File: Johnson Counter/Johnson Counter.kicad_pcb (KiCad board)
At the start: 2 copper layers, 149.9 x 114.3 mm, 52 parts, among them J101 USB_A, SW601 SW_Push, U201 74HC74, U301 74HC74, U401 74HC74, U501 74HC74, U601 LM555xM, U701 4081, U702 4081

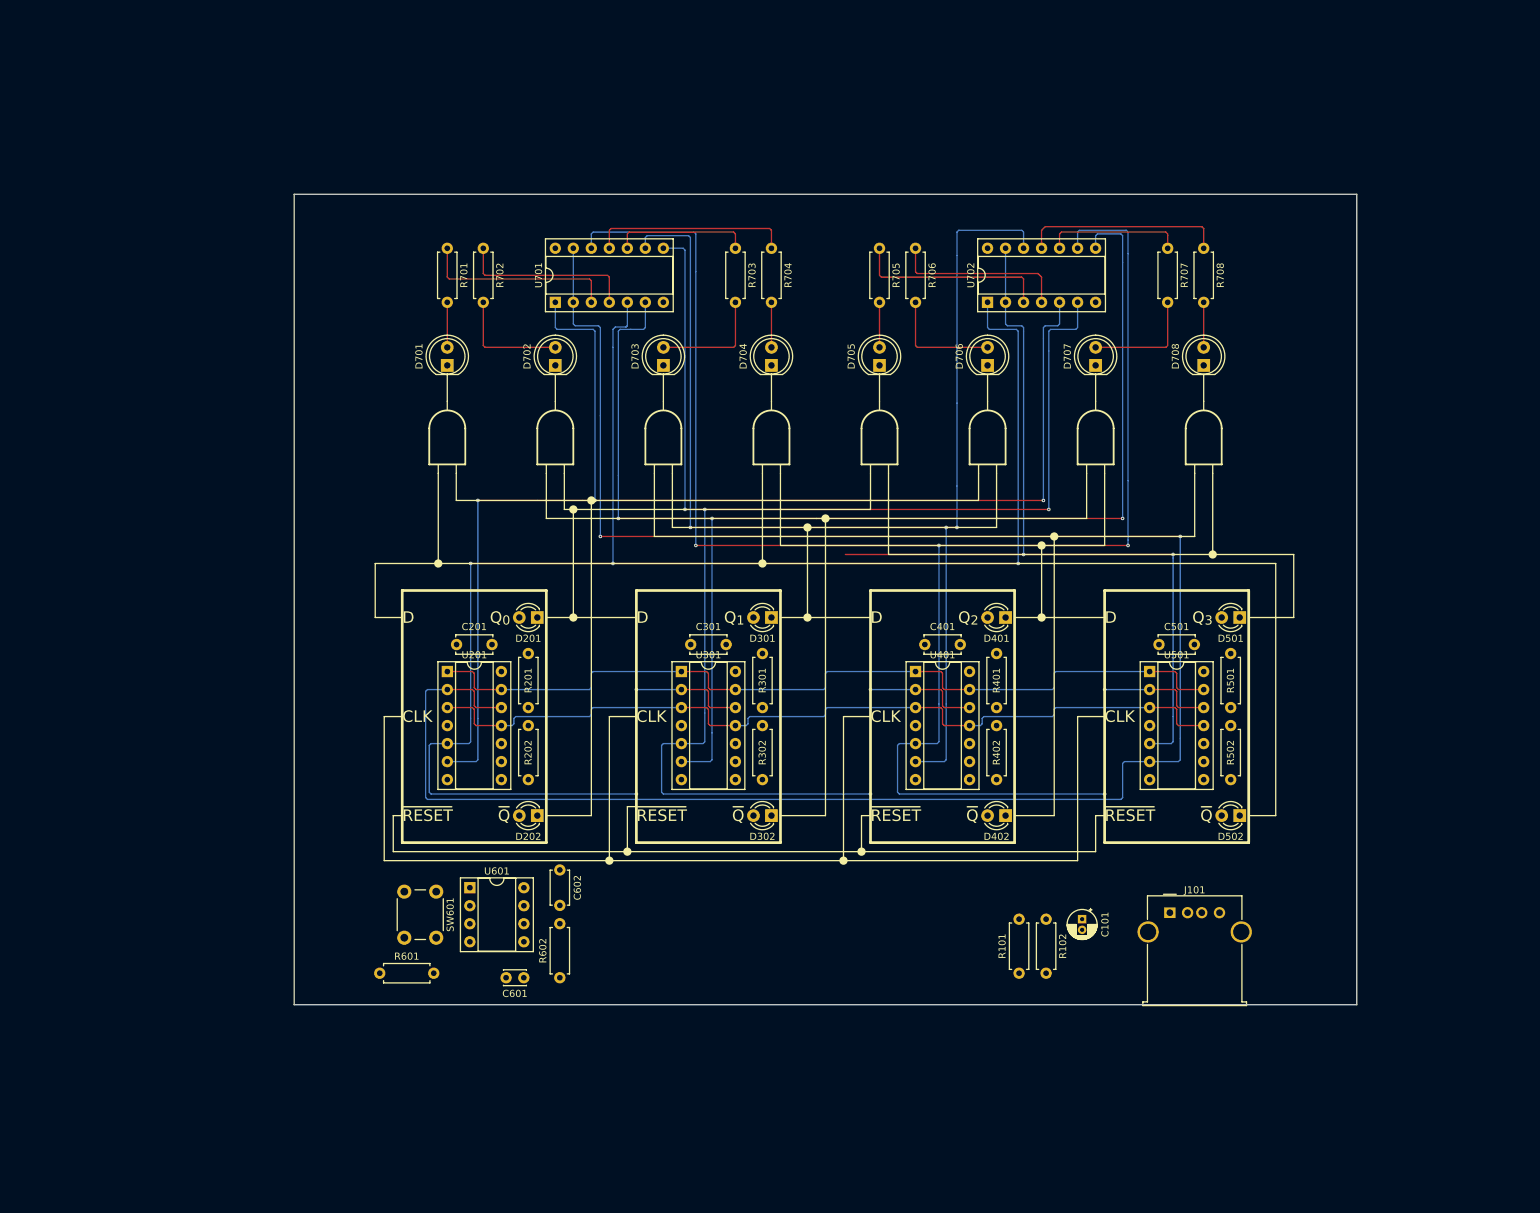
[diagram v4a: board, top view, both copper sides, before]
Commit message: Finishing routing, silkscreen and mounting
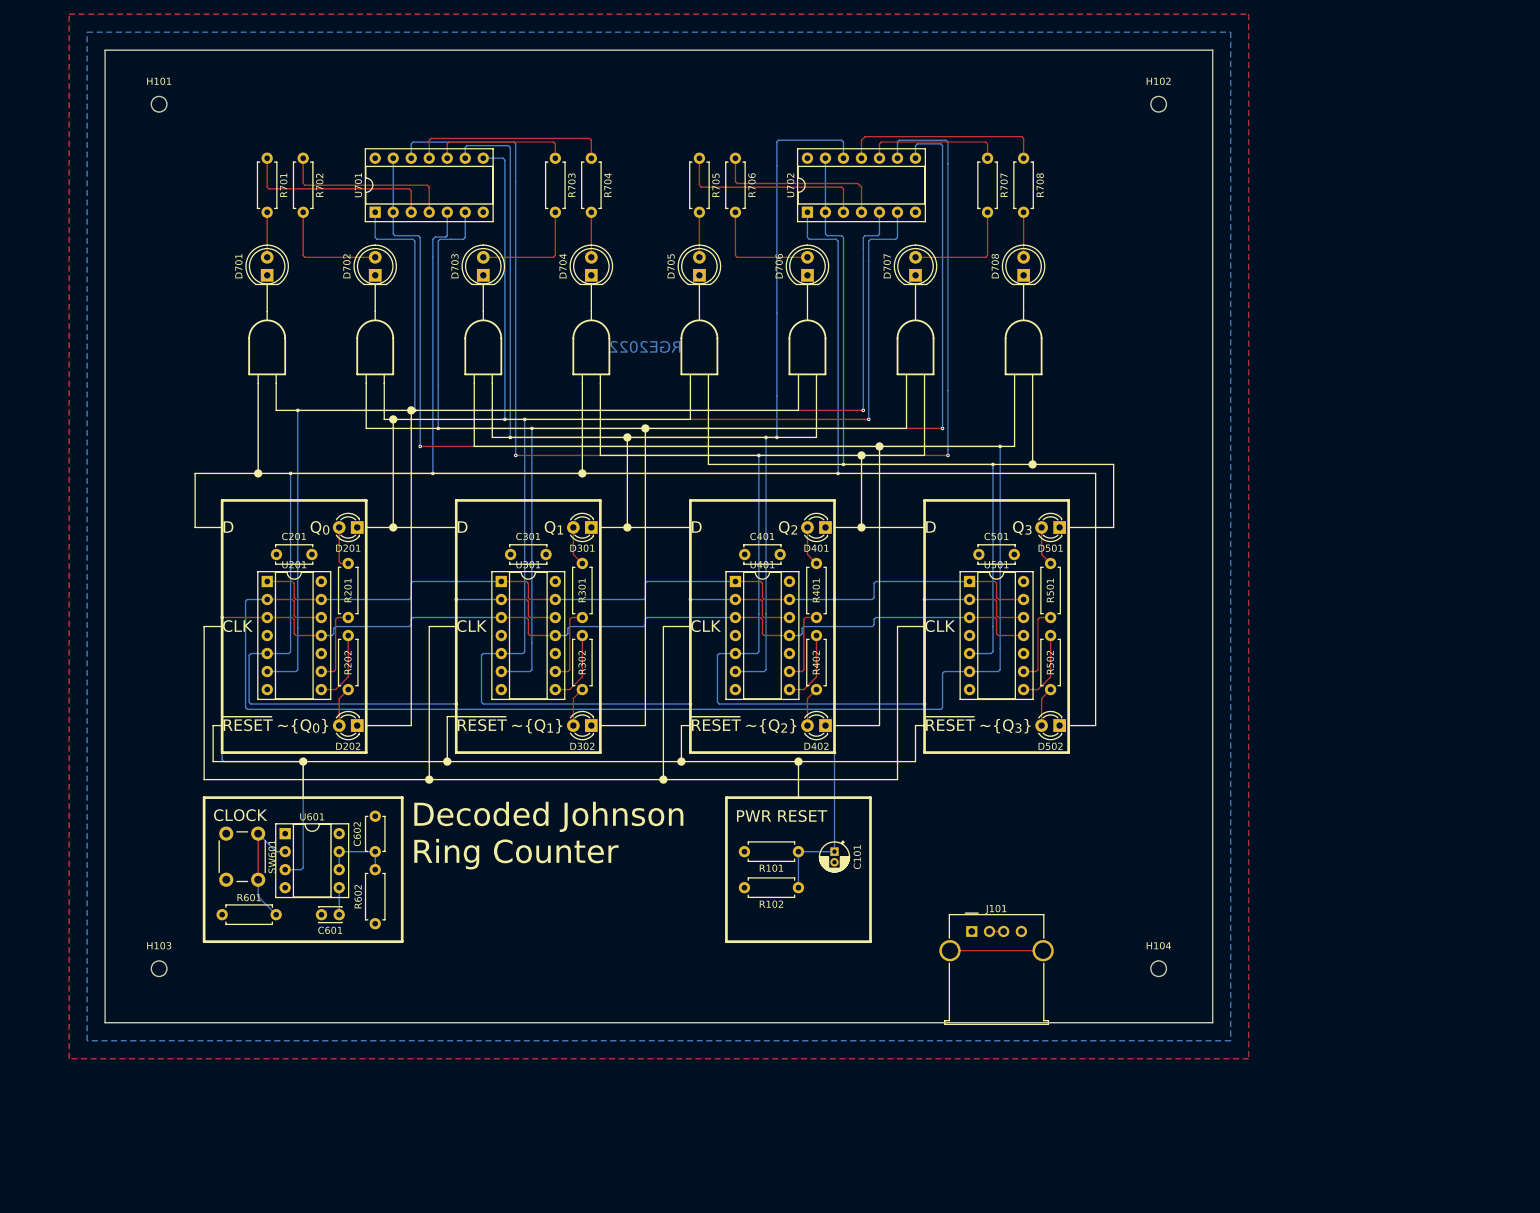
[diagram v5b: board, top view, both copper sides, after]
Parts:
- added H101: MountingHole, MountingHole:MountingHole_2.2mm_M2, F.Cu at (85.1, 31.8)
- added H102: MountingHole, MountingHole:MountingHole_2.2mm_M2, F.Cu at (226.1, 31.8)
- added H103: MountingHole, MountingHole:MountingHole_2.2mm_M2, F.Cu at (85.1, 153.7)
- added H104: MountingHole, MountingHole:MountingHole_2.2mm_M2, F.Cu at (226.1, 153.7)
- moved C101 36.2 mm to (180.3, 137.2)
- moved R101 35.5 mm to (175.3, 137.2), turned to 180 degrees
- moved R102 35.2 mm to (175.3, 142.2), turned to 180 degrees
- moved D202 28.4 mm to (113.0, 119.4)
- moved D402 28.4 mm to (179.1, 119.4)
- moved D502 28.4 mm to (212.1, 119.4)
- moved C201 28.4 mm to (101.6, 95.2)
- moved C301 28.4 mm to (134.7, 95.2)
- moved C401 28.4 mm to (167.7, 95.2)
- moved C501 28.4 mm to (200.7, 95.2)
- moved D201 28.4 mm to (113.0, 91.4)
- moved D401 28.4 mm to (179.1, 91.4)
- moved D501 28.4 mm to (212.1, 91.4)
- moved R301 28.4 mm to (144.8, 104.1)
- moved R501 28.4 mm to (210.8, 104.1)
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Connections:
- C602 pad 1: GND -> Net-(R602-Pad2)
- C602 pad 2: Net-(C602-Pad2) -> GND
- R101 pad 1: +5V -> /~{RESET}
- R101 pad 2: /~{RESET} -> +5V
- R602 pad 2: Net-(C602-Pad2) -> Net-(R602-Pad2)
- U601 pad 6: Net-(C602-Pad2) -> Net-(R602-Pad2)
- U601 pad 7: Net-(C602-Pad2) -> Net-(R602-Pad2)
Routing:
- net /CLOCK: track 121.5 -> 176.9 mm, vias 0 -> 1
- net /~{RESET}: track 122.4 -> 168.1 mm, vias 0 -> 2
- net /Q_{3}: track 121.5 -> 96.3 mm
- net Net-(R601-Pad2): track 0.00 -> 17.3 mm
- net unconnected-(J101-Pad5): track 0.00 -> 13.1 mm
- net Net-(R501-Pad1): track 0.00 -> 11.1 mm
- net Net-(R401-Pad1): track 0.00 -> 11.1 mm
- net Net-(R301-Pad1): track 0.00 -> 11.1 mm
- net Net-(R201-Pad1): track 0.00 -> 11.1 mm
- net Net-(R502-Pad1): track 0.00 -> 10.4 mm
- net Net-(R302-Pad1): track 0.00 -> 10.4 mm
- net Net-(R402-Pad1): track 0.00 -> 10.4 mm
- net Net-(R202-Pad1): track 0.00 -> 10.4 mm
- net Net-(R602-Pad2): track 0.00 -> 10.2 mm
- net Net-(D201-Pad2): track 0.00 -> 6.20 mm
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- added copper zone on B.Cu, net +5V
- added copper zone on F.Cu, net GND
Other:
- board size 149.9 x 114.3 mm -> 156.2 x 137.2 mm
- board text added: "CLOCK"
- board text added: "Decoded Johnson Ring Counter"
- board text added: "PWR RESET"
- board text added: "RGE2022"
- board text added: "~{Q_{0}}"
- board text added: "~{Q_{1}}"
- board text added: "~{Q_{2}}"
- board text added: "~{Q_{3}}"
- board text removed: "~{Q}"

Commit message: Forgot to add order locator
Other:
- board text added: "JLCJLCJLCJLC"
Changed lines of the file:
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@@
       (layerselection 0x00010fc_ffffffff)
       (disableapertmacros false)
-      (usegerberextensions false)
+      (usegerberextensions true)
       (usegerberattributes true)
       (usegerberadvancedattributes true)
-      (creategerberjobfile true)
+      (creategerberjobfile false)
       (svguseinch false)
       (svgprecision 6)
@@
       (psa4output false)
       (plotreference true)
-      (plotvalue true)
+      (plotvalue false)
       (plotinvisibletext false)
       (sketchpadsonfab false)
-      (subtractmaskfromsilk false)
+      (subtractmaskfromsilk true)
       (outputformat 1)
       (mirror false)
-      (drillshape 1)
+      (drillshape 0)
       (scaleselection 1)
-      (outputdirectory "")
+      (outputdirectory "gerbers/")
     )
   )
@@
     (effects (font (size 1.6256 1.6256) (thickness 0.3048)) (justify mirror))
   )
+  (gr_text "JLCJLCJLCJLC" (at 203.2 157.48) (layer "B.SilkS")
+    (effects (font (size 1 1) (thickness 0.15)) (justify mirror))
+  )
   (gr_text "CLK" (at 93.98 105.41) (layer "F.SilkS")
